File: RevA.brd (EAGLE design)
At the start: 106 x 53 mm, 62 parts, among them IC1 MAX31855, IC10 DS3231/SO, IC3 MAX31855, IC4 MAX31855, IC5 MAX31855, IC9 ATMEGA32U4-AU, J1 1X2-3.5MM, J2 1X2-3.5MM, J3 1X2-3.5MM, J4 1X2-3.5MM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

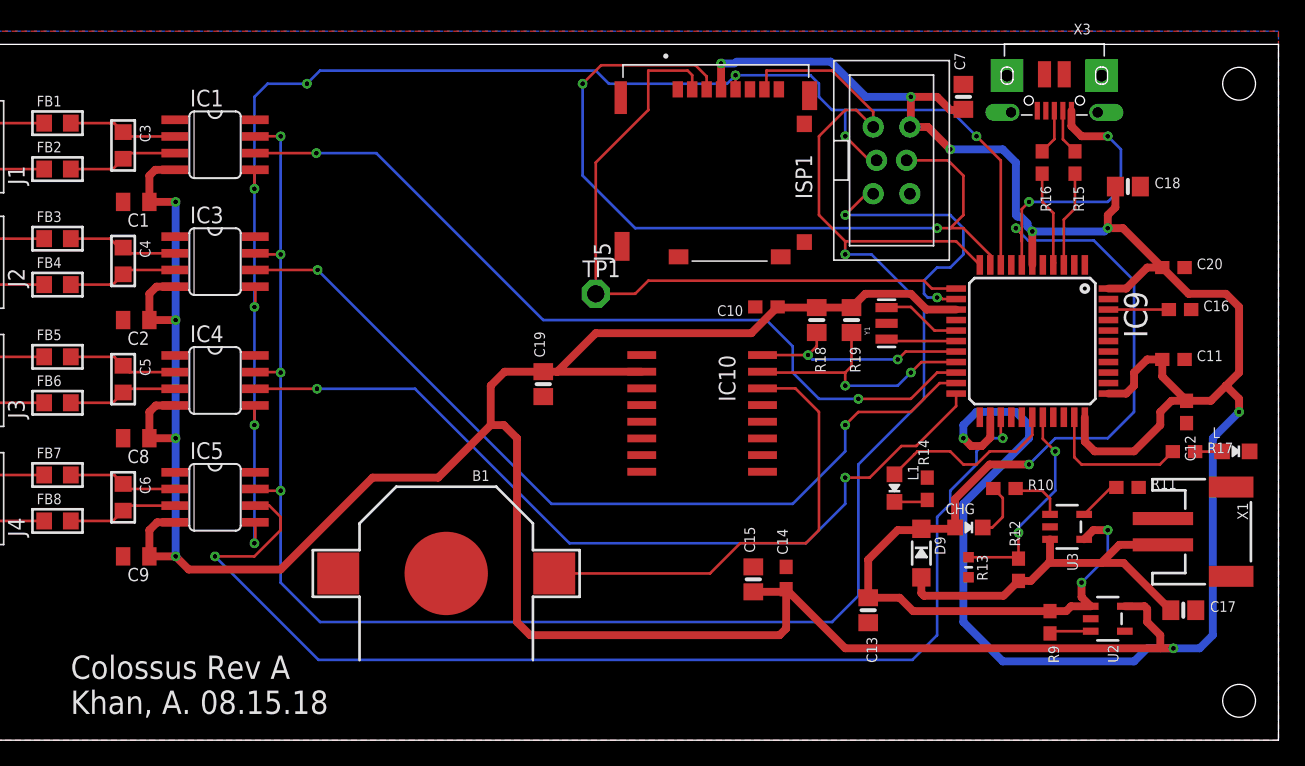
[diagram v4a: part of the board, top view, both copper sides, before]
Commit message: Minor cosmetic changes
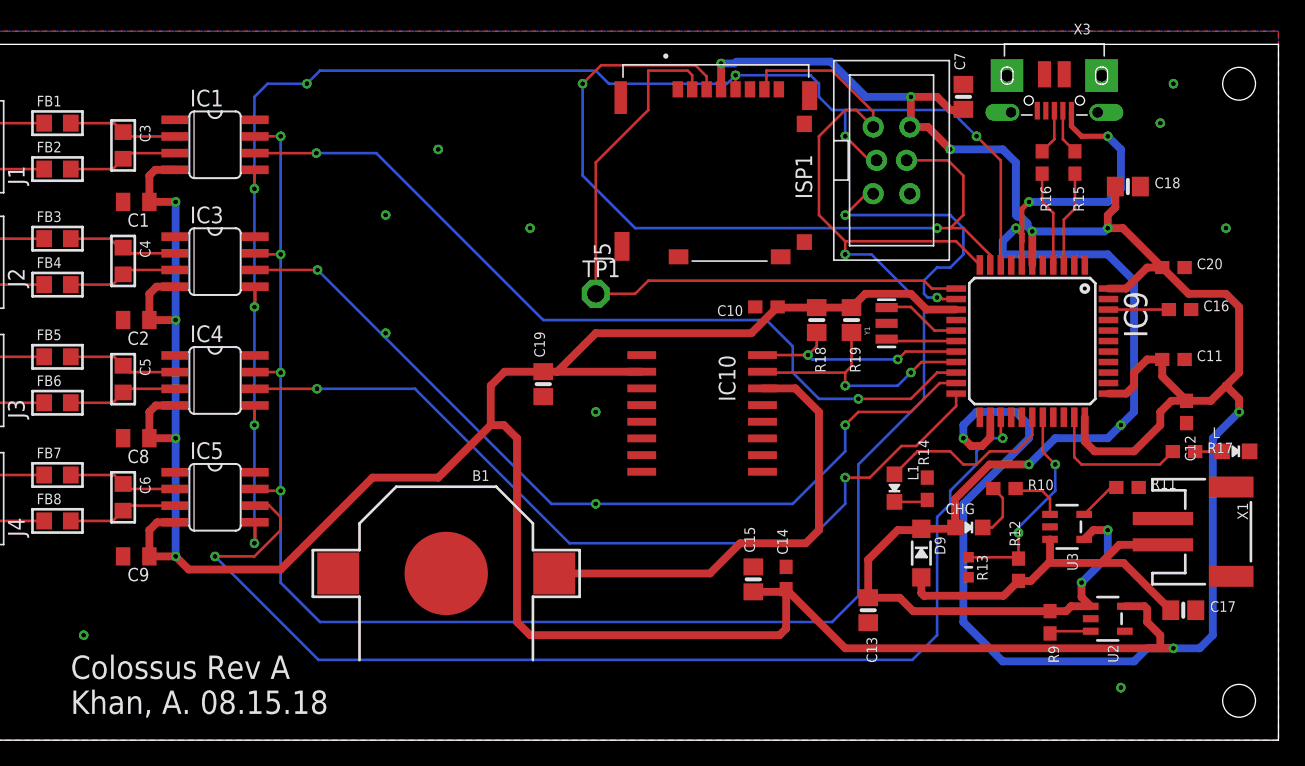
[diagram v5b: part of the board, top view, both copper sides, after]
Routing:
- net VBUS: track 98.6 -> 101.2 mm, vias 6 -> 7
- net CS-2: vias 2 -> 3
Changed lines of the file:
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@@
 <layer number="14" name="Route14" color="22" fill="1" visible="no" active="no"/>
 <layer number="15" name="Route15" color="23" fill="1" visible="no" active="no"/>
-<layer number="16" name="Bottom" color="1" fill="1" visible="no" active="yes"/>
+<layer number="16" name="Bottom" color="1" fill="1" visible="yes" active="yes"/>
 <layer number="17" name="Pads" color="2" fill="1" visible="yes" active="yes"/>
 <layer number="18" name="Vias" color="2" fill="1" visible="yes" active="yes"/>
@@
 </layers>
 <board>
-<fusionsync huburn="a.cGVyc29uYWw6dWUyYmRkYjQx" projecturn="a.cGVyc29uYWw6dWUyYmRkYjQxIzIwMTgwNTAyMTMwMjU4MzAx" f3durn="urn:adsk.wipprod:dm.lineage:a68wfmUxQy2LyGLi9FcYGg" pcbguid="62a8e096-691a-4df0-bd8f-1dbb8bf064d3" lastpulledtime="" lastsyncedchangeguid="8f3f0e9c-4609-a4f6-33ee-2cdfbfc5844f"/>
+<fusionsync huburn="a.cGVyc29uYWw6dWUyYmRkYjQx" projecturn="a.cGVyc29uYWw6dWUyYmRkYjQxIzIwMTgwNTAyMTMwMjU4MzAx" f3durn="urn:adsk.wipprod:dm.lineage:a68wfmUxQy2LyGLi9FcYGg" pcbguid="62a8e096-691a-4df0-bd8f-1dbb8bf064d3" lastpulledtime="" lastsyncedchangeguid="c89f0ef9-c541-d99c-1cd4-87cf159fafcb"/>
 <plain>
 <wire x1="0" y1="0" x2="106" y2="0" width="0" layer="20"/>
@@
 <contactref element="X3" pad="VBUS"/>
 <contactref element="IC9" pad="7"/>
-<wire x1="90.23" y1="47.945" x2="90.23" y2="46.77" width="0.6" layer="1"/>
-<wire x1="90.23" y1="46.77" x2="91" y2="46" width="0.6" layer="1"/>
-<wire x1="91" y1="46" x2="93" y2="46" width="0.6" layer="1"/>
 <via x="93" y="46" extent="1-16" drill="0.35"/>
-<wire x1="93" y1="46" x2="94" y2="45" width="0.2032" layer="16"/>
-<wire x1="94" y1="45" x2="94" y2="42" width="0.2032" layer="16"/>
-<wire x1="94" y1="42" x2="93" y2="41" width="0.2032" layer="16"/>
-<wire x1="93" y1="41" x2="87" y2="41" width="0.2032" layer="16"/>
+<wire x1="93" y1="46" x2="94" y2="45" width="0.6" layer="16"/>
+<wire x1="94" y1="45" x2="94" y2="42" width="0.6" layer="16"/>
+<wire x1="94" y1="42" x2="93" y2="41" width="0.6" layer="16"/>
+<wire x1="93" y1="41" x2="87" y2="41" width="0.6" layer="16"/>
 <via x="87" y="41" extent="1-16" drill="0.35"/>
-<wire x1="86.45" y1="36.2" x2="86.45" y2="38" width="0.2032" layer="1"/>
-<wire x1="86.45" y1="38" x2="86.45" y2="40.45" width="0.2032" layer="1"/>
-<wire x1="86.45" y1="40.45" x2="87" y2="41" width="0.2032" layer="1"/>
+<wire x1="86.45" y1="36.2" x2="86.45" y2="38" width="0.4" layer="1"/>
+<wire x1="86.45" y1="38" x2="86.45" y2="40.45" width="0.4" layer="1"/>
+<wire x1="86.45" y1="40.45" x2="87" y2="41" width="0.4" layer="1"/>
 <wire x1="78.8" y1="16.1" x2="81.27" y2="16.1" width="0.6" layer="1"/>
 <wire x1="81.27" y1="16.1" x2="81.37" y2="16.2" width="0.2032" layer="1"/>
@@
 <wire x1="84" y1="21" x2="87" y2="21" width="0.6" layer="1"/>
 <via x="87" y="21" extent="1-16" drill="0.35"/>
-<wire x1="87" y1="21" x2="89" y2="23" width="0.2032" layer="16"/>
-<wire x1="93" y1="23" x2="95" y2="25" width="0.2032" layer="16"/>
-<wire x1="95" y1="25" x2="95" y2="35" width="0.2032" layer="16"/>
+<wire x1="87" y1="21" x2="89" y2="23" width="0.6" layer="16"/>
+<wire x1="93" y1="23" x2="94" y2="24" width="0.6" layer="16"/>
+<wire x1="94" y1="24" x2="95" y2="25" width="0.6" layer="16"/>
+<wire x1="95" y1="25" x2="95" y2="35" width="0.6" layer="16"/>
 <wire x1="81.37" y1="18.37" x2="84" y2="21" width="0.6" layer="1"/>
-<wire x1="89" y1="23" x2="93" y2="23" width="0.2032" layer="16"/>
-<wire x1="95" y1="35" x2="91.933" y2="38.067" width="0.2032" layer="16"/>
-<wire x1="91.933" y1="38.067" x2="86.933" y2="38.067" width="0.2032" layer="16"/>
-<wire x1="86.933" y1="38.067" x2="86" y2="39" width="0.2032" layer="16"/>
+<wire x1="89" y1="23" x2="93" y2="23" width="0.6" layer="16"/>
+<wire x1="95" y1="35" x2="93" y2="37" width="0.6" layer="16"/>
 <via x="86" y="39" extent="1-16" drill="0.35"/>
 <wire x1="91.2001" y1="15.3" x2="91.9001" y2="16" width="0.6" layer="1"/>
 <wire x1="91.9001" y1="16" x2="93" y2="16" width="0.6" layer="1"/>
 <via x="93" y="16" extent="1-16" drill="0.35"/>
-<wire x1="93" y1="16" x2="93" y2="14" width="0.2032" layer="16"/>
-<wire x1="93" y1="14" x2="91" y2="12" width="0.2032" layer="16"/>
+<wire x1="93" y1="16" x2="93" y2="14" width="0.6" layer="16"/>
+<wire x1="93" y1="14" x2="91" y2="12" width="0.6" layer="16"/>
 <via x="91" y="12" extent="1-16" drill="0.35"/>
 <wire x1="91" y1="12" x2="91.000003125" y2="10.899896875" width="0.6" layer="1"/>
 <wire x1="91.000003125" y1="10.899896875" x2="91.6999" y2="10.2" width="0.6" layer="1"/>
-<wire x1="86" y1="39" x2="86.45" y2="38.55" width="0.2032" layer="1"/>
-<wire x1="86.45" y1="38.55" x2="86.45" y2="38" width="0.2032" layer="1"/>
+<wire x1="86" y1="39" x2="86.45" y2="38.55" width="0.4" layer="1"/>
+<wire x1="86.45" y1="38.55" x2="86.45" y2="38" width="0.4" layer="1"/>
+<wire x1="90.23" y1="47.945" x2="90.23" y2="46.77" width="0.4" layer="1"/>
+<wire x1="90.23" y1="46.77" x2="91" y2="46" width="0.4" layer="1"/>
+<wire x1="91" y1="46" x2="93" y2="46" width="0.4" layer="1"/>
+<wire x1="86" y1="39" x2="85" y2="38" width="0.6" layer="16"/>
+<wire x1="85" y1="38" x2="85" y2="37" width="0.6" layer="16"/>
+<wire x1="85" y1="37" x2="93" y2="37" width="0.6" layer="16"/>
+<via x="94" y="24" extent="1-16" drill="0.35"/>
 </signal>
 <signal name="VBAT">
@@
 <wire x1="97.8" y1="9.9" x2="94.2" y2="13.5" width="0.6" layer="1"/>
 <wire x1="94.2" y1="13.5" x2="92.5" y2="13.5" width="0.6" layer="1"/>
-<wire x1="50.8354" y1="12.7" x2="62.7" y2="12.7" width="0.2032" layer="1"/>
-<wire x1="65" y1="15" x2="70" y2="15" width="0.2032" layer="1"/>
-<wire x1="70" y1="15" x2="71" y2="16" width="0.2032" layer="1"/>
-<wire x1="69.205" y1="26.795" x2="66.7" y2="26.795" width="0.2032" layer="1"/>
-<wire x1="62.7" y1="12.7" x2="65" y2="15" width="0.2032" layer="1"/>
-<wire x1="71" y1="16" x2="71" y2="25" width="0.2032" layer="1"/>
-<wire x1="71" y1="25" x2="69.205" y2="26.795" width="0.2032" layer="1"/>
+<wire x1="50.8354" y1="12.7" x2="62.7" y2="12.7" width="0.6" layer="1"/>
+<wire x1="65" y1="15" x2="70" y2="15" width="0.6" layer="1"/>
+<wire x1="70" y1="15" x2="71" y2="16" width="0.6" layer="1"/>
+<wire x1="69.205" y1="26.795" x2="66.7" y2="26.795" width="0.6" layer="1"/>
+<wire x1="62.7" y1="12.7" x2="65" y2="15" width="0.6" layer="1"/>
+<wire x1="71" y1="16" x2="71" y2="25" width="0.6" layer="1"/>
+<wire x1="71" y1="25" x2="69.205" y2="26.795" width="0.6" layer="1"/>
 <wire x1="71" y1="16" x2="78.8" y2="12.4" width="0" layer="19" extent="1-1"/>
 </signal>
@@
 <wire x1="86.098" y1="13.932" x2="86.199996875" y2="13.830003125" width="0.2032" layer="1"/>
 <wire x1="86.2" y1="13.83" x2="86.2" y2="15.8" width="0.2032" layer="1"/>
-<wire x1="89" y1="19" x2="89" y2="22" width="0.2032" layer="16"/>
-<via x="89" y="22" extent="1-16" drill="0.35"/>
-<wire x1="88.05" y1="24.6" x2="88.05" y2="22.95" width="0.2032" layer="1"/>
-<wire x1="88.05" y1="22.95" x2="89" y2="22" width="0.2032" layer="1"/>
 <via x="86.2" y="15.8" extent="1-16" drill="0.35"/>
 <wire x1="86.2" y1="15.8" x2="86.2" y2="16.2" width="0.2032" layer="16"/>
 <wire x1="86.2" y1="16.2" x2="89" y2="19" width="0.2032" layer="16"/>
+<wire x1="88.05" y1="21.95" x2="89" y2="21" width="0.2032" layer="1"/>
+<via x="89" y="21" extent="1-16" drill="0.35"/>
+<wire x1="88.05" y1="24.6" x2="88.05" y2="21.95" width="0.2032" layer="1"/>
+<wire x1="89" y1="19" x2="89" y2="21" width="0.2032" layer="16"/>
 <wire x1="86.199996875" y1="13.830003125" x2="86.2" y2="13.83" width="0" layer="19" extent="1-1"/>
 </signal>
@@
 <via x="73" y="24" extent="1-16" drill="0.35"/>
 <wire x1="32.815" y1="35.815" x2="50.63" y2="18" width="0.2032" layer="16"/>
-<wire x1="50.63" y1="18" x2="69" y2="18" width="0.2032" layer="16"/>
+<wire x1="50.63" y1="18" x2="54" y2="18" width="0.2032" layer="16"/>
+<wire x1="54" y1="18" x2="69" y2="18" width="0.2032" layer="16"/>
 <wire x1="69" y1="18" x2="73" y2="22" width="0.2032" layer="16"/>
 <wire x1="73" y1="22" x2="73" y2="24" width="0.2032" layer="16"/>
+<via x="54" y="18" extent="1-16" drill="0.35"/>
 </signal>
 <signal name="CS-3">
@@
 <wire x1="84" y1="23" x2="85" y2="23" width="0.2032" layer="16"/>
 </signal>
+<signal name="N$17">
+<via x="42" y="45" extent="1-16" drill="0.35"/>
+</signal>
+<signal name="N$18">
+<via x="49" y="39" extent="1-16" drill="0.35"/>
+</signal>
+<signal name="N$19">
+<via x="38" y="31" extent="1-16" drill="0.35"/>
+</signal>
+<signal name="N$20">
+<via x="38" y="40" extent="1-16" drill="0.35"/>
+</signal>
+<signal name="N$21">
+<via x="54" y="25" extent="1-16" drill="0.35"/>
+</signal>
+<signal name="N$22">
+<via x="94" y="4" extent="1-16" drill="0.35"/>
+</signal>
+<signal name="N$23">
+<via x="102" y="39" extent="1-16" drill="0.35"/>
+</signal>
+<signal name="N$24">
+<via x="97" y="47" extent="1-16" drill="0.35"/>
+</signal>
+<signal name="N$34">
+<via x="98" y="50" extent="1-16" drill="0.35"/>
+</signal>
+<signal name="N$35">
+<via x="15" y="8" extent="1-16" drill="0.35"/>
+</signal>
 </signals>

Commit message: More Revision
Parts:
- removed R9: 100k, microbuilder:0603-NO
- moved C7 32.0 mm to (50.0, 50.0), turned to 180 degrees
- moved C13 13.2 mm to (87.9, 9.25), turned to 180 degrees
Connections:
- removed net EN: R9.2, U2.3
- new net COIN: B1.+$1, IC10.14
- net VBAT: no longer B1.+$1, IC10.14
- net VBUS: now also U2.3; no longer R9.1
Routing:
- net VBAT: track 65.5 -> 29.9 mm
- net COIN: track 0.00 -> 35.6 mm
- net VBUS: track 101.2 -> 81.9 mm, vias 7 -> 6
- net +3V3: track 378.0 -> 372.7 mm, vias 12 -> 13
- net EN: track 3.17 -> 0.00 mm
- net SCK: track 116.0 -> 114.6 mm, vias 8 -> 7

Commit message: Changed Layout
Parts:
- moved C14 46.5 mm to (104.0, 42.4)
- moved C15 45.5 mm to (102.8, 39.0)
- moved CHG 29.5 mm to (99.9, 40.0), turned to 90 degrees
- moved U2 27.5 mm to (102.0, 35.2)
- moved D9 26.3 mm to (101.8, 27.0), turned to 180 degrees
- moved C13 25.5 mm to (102.7, 30.0)
- moved U3 23.3 mm to (93.9, 39.2), turned to 90 degrees
- moved R10 23.1 mm to (98.0, 38.3), turned to 180 degrees
- moved R17 21.9 mm to (89.8, 2.00)
- moved L 20.6 mm to (98.0, 2.00)
- moved L1 19.0 mm to (84.8, 2.00), turned to 90 degrees
- moved R14 17.2 mm to (81.0, 2.00), turned to 180 degrees
- moved R11 17.0 mm to (93.5, 36.2)
- moved C17 11.1 mm to (94.0, 19.9), turned to 270 degrees
- moved C10 11.0 mm to (78.0, 33.0)
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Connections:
- net COIN renamed VCR
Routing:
- net +3V3: track 372.7 -> 254.6 mm, vias 13 -> 11
- net VBUS: track 81.9 -> 46.5 mm, vias 6 -> 3
- net 13: track 11.2 -> 23.3 mm, vias 0 -> 2
- net VBAT: track 29.9 -> 40.9 mm, vias 0 -> 2
- net 8: track 13.9 -> 23.8 mm
- net 9: track 16.2 -> 7.25 mm, vias 2 -> 0
- net MISO: track 158.0 -> 153.0 mm
- net N$33: track 2.62 -> 6.32 mm
- net MOSI: track 61.9 -> 65.1 mm
- net N$25: track 4.33 -> 1.70 mm
- net SDA: track 19.8 -> 17.3 mm, vias 2 -> 0
- net N$26: track 4.14 -> 1.95 mm
- net SCL: track 17.1 -> 15.1 mm
- net RST: track 21.7 -> 20.4 mm
- net N$27: track 3.30 -> 2.07 mm
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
